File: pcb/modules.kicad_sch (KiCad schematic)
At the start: 12 parts, among them IC2 E22-900M22S, J2 Conn_01x08_Pin, J3 Conn_Coaxial, J4 Conn_Coaxial, U4 BME280, U6 NEO-M8M

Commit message: Updating schematic & pcb & BOM
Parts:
- J3: footprint (none) -> Connector_Coaxial:U.FL_Hirose_U.FL-R-SMT-1_Vertical
- L2: footprint (none) -> Inductor_SMD:L_0805_2012Metric
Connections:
- net +3V3: now also J2.7 (Pin_7)
- net GND: now also J2.8 (Pin_8)
- net SCL: now also J2.6 (Pin_6)
- net SDA: now also J2.5 (Pin_5)
- net BLK: now reaches J2.1 (Pin_1)
- net CS: now reaches J2.2 (Pin_2)
- net DC: now reaches J2.3 (Pin_3)
- net RES: now reaches J2.4 (Pin_4)
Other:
- title: (none) -> NOMAD MODULES
- moved on the sheet: C9, D2, IC2, J2, J3, J4, L2, R14, R16, R17, U4, U6

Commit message: Updating PCB
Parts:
- added Q1: NPN, symbol Simulation_SPICE:NPN
- added R1: R, symbol Device:R
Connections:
- net +3V3: now also IC2.9 (VCC), R1.2
- net GND: now also D2.1 (K), J4.2 (Ext)
- net at D2.2 (A): now also Q1.3 (E)
- new net: Q1.1 (C), R1.1
- new net FLASHLIGHT: Q1.2 (B)
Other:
- moved on the sheet: D2

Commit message: Updating footprints, PCb and schematics.
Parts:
- R1: footprint (none) -> Resistor_SMD:R_0805_2012Metric
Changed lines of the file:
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@@
 			)
 		)
-		(property "Footprint" ""
+		(property "Footprint" "Resistor_SMD:R_0805_2012Metric"
 			(at 201.422 144.78 90)
 			(hide yes)

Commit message: Updating PCB
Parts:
- removed Q1: NPN, symbol Simulation_SPICE:NPN
- added Q2: 2N7002, Package_TO_SOT_SMD:SOT-23, symbol Transistor_FET:2N7002
- added R19: 100R, symbol Device:R
- R1: value R -> 1.5k
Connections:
- net +3V3: now also D2.1 (K); no longer R1.2
- net FLASHLIGHT: now also R19.2
- net GND: now also R1.1; no longer D2.1 (K)
- net at D2.2 (A): now also Q2.3 (D)
- new net: Q2.2 (S), R1.2
- new net: Q2.1 (G), R19.1
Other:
- moved on the sheet: D2, R1

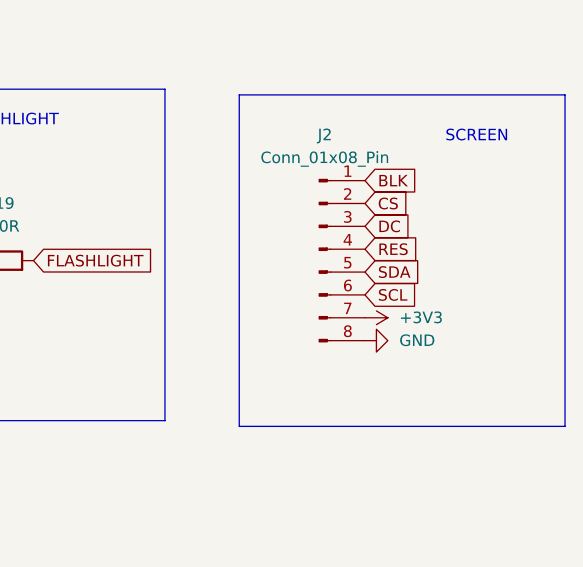
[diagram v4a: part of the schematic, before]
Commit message: Updating PCB: Adding Buck boost converter, battery protection and other fixes.
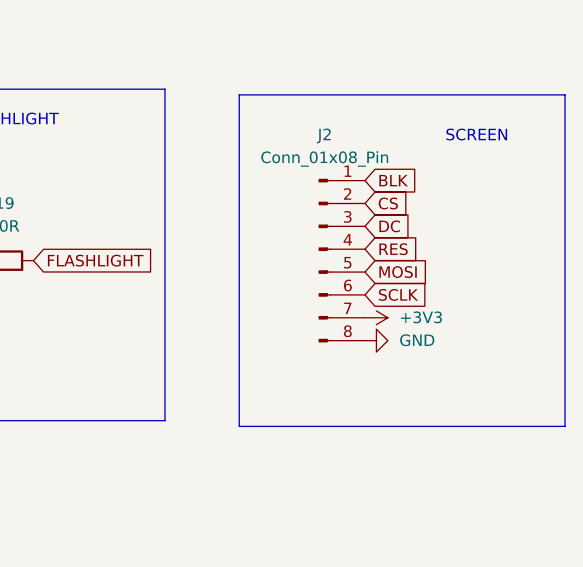
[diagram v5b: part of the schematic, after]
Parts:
- R19: footprint (none) -> Resistor_SMD:R_0805_2012Metric
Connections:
- net SCL: no longer J2.6 (Pin_6)
- net SDA: no longer J2.5 (Pin_5)
- new net MOSI: J2.5 (Pin_5)
- new net SCLK: J2.6 (Pin_6)

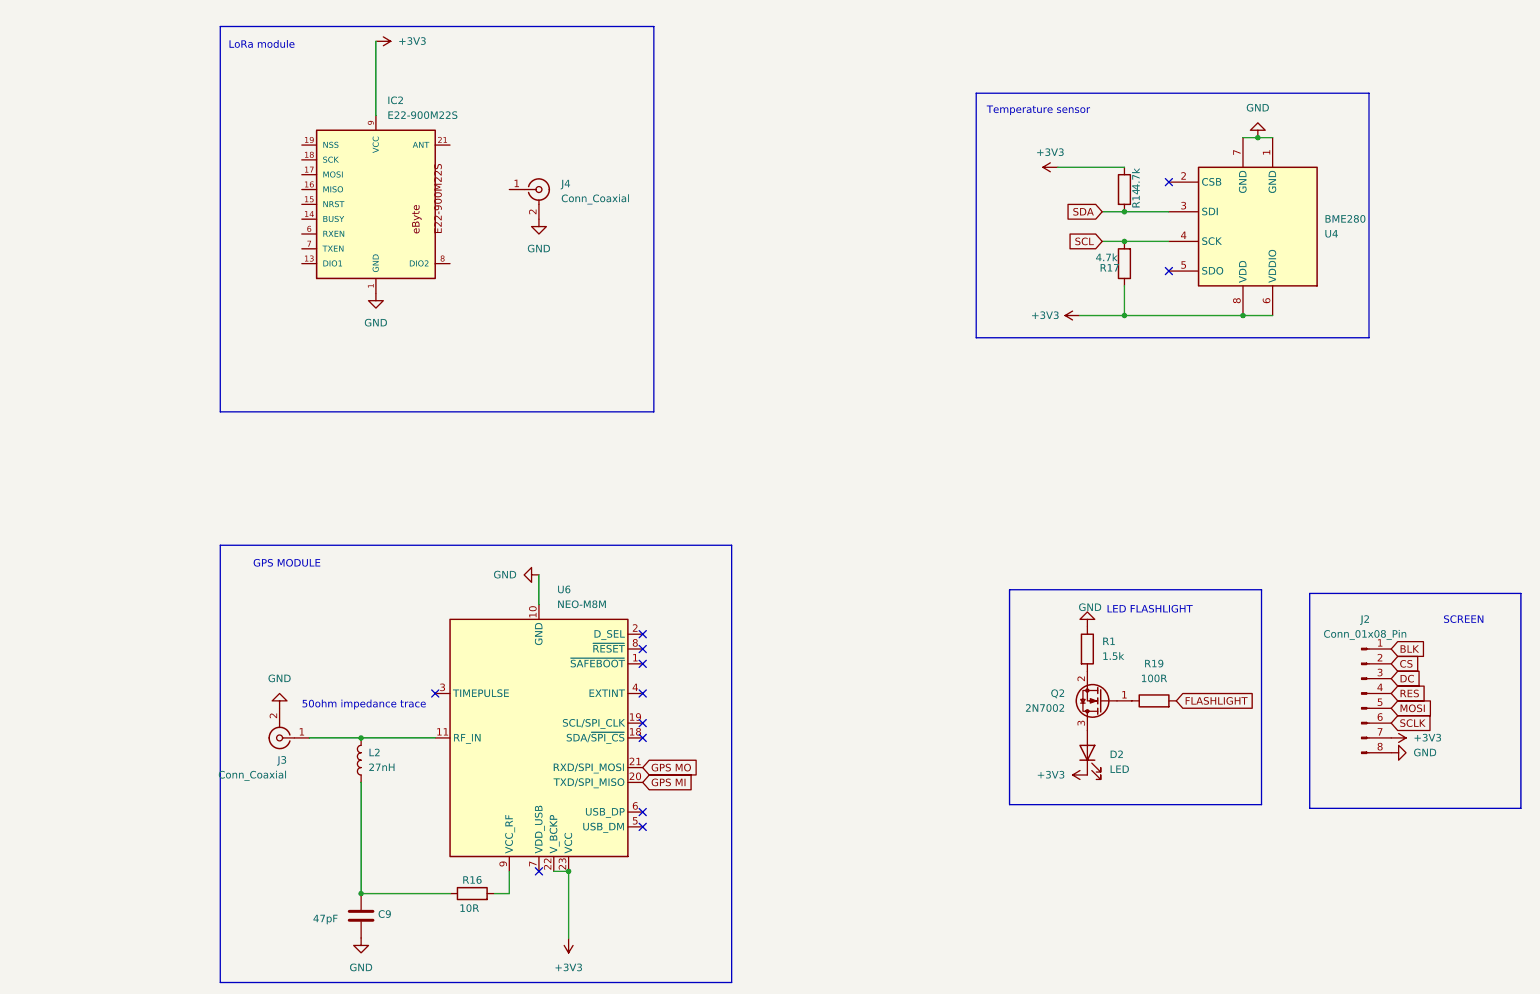
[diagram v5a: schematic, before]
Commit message: Adding NEO-M8N module schematic + BME280 schematic
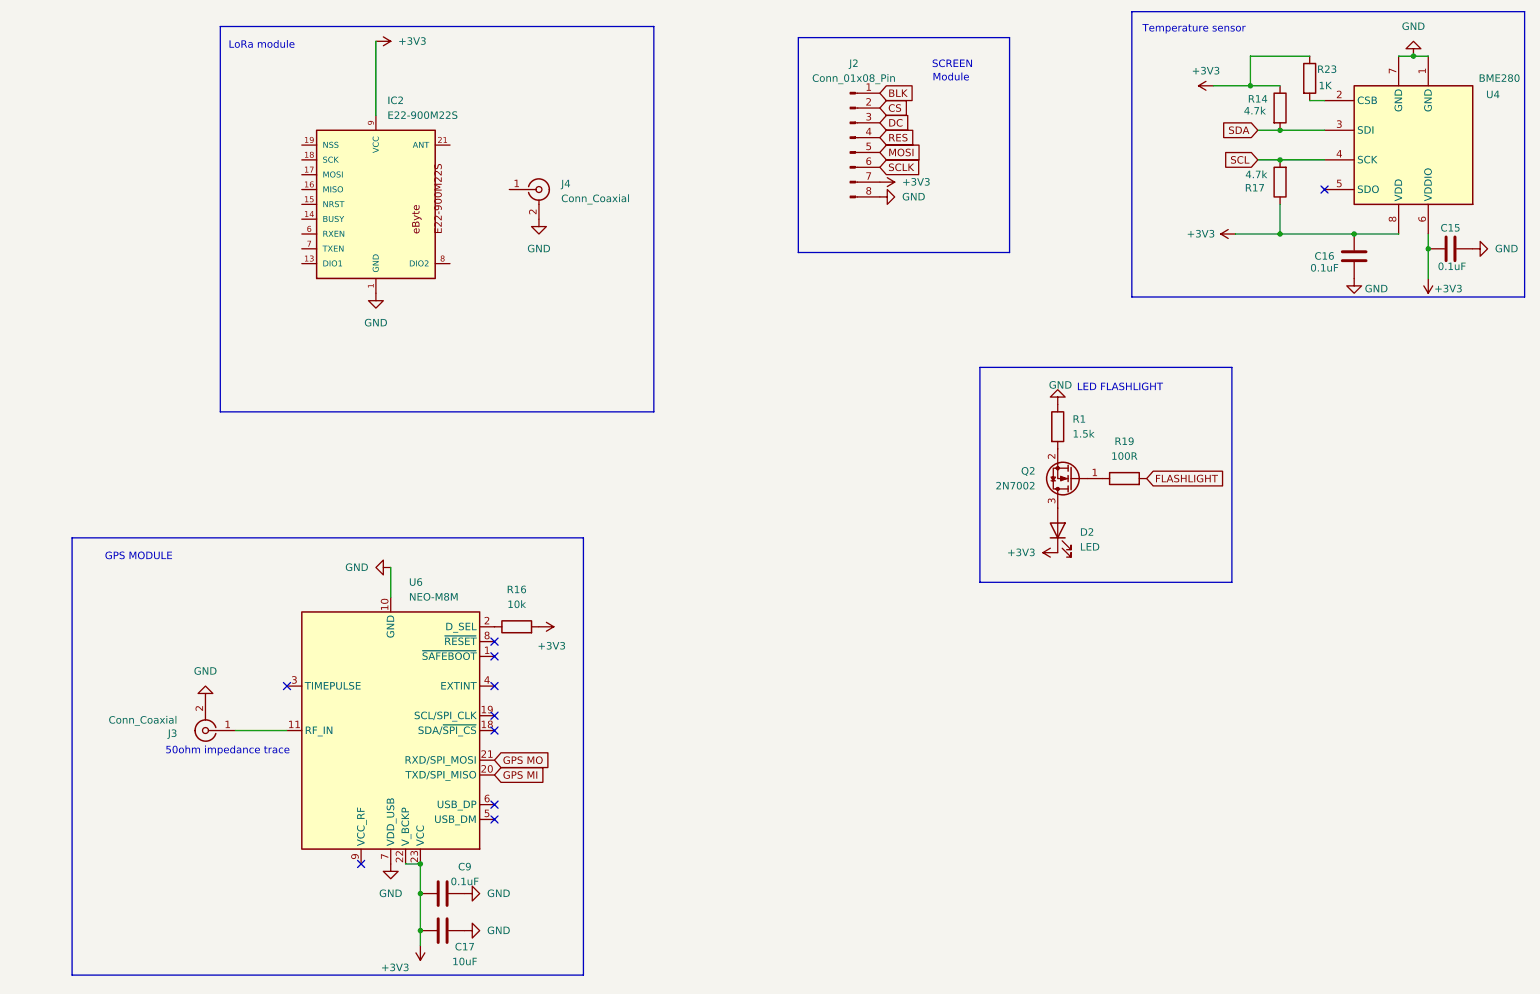
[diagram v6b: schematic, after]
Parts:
- removed L2: 27nH, Inductor_SMD:L_0805_2012Metric, symbol Device:L
- added C15, C16: 0.1uF, symbol Device:C
- added C17: 10uF, symbol Device:C
- added R23: 1K, symbol Device:R
- C9: value 47pF -> 0.1uF; footprint Capacitor_SMD:C_0805_2012Metric -> (none)
- J3: footprint Connector_Coaxial:U.FL_Hirose_U.FL-R-SMT-1_Vertical -> Connector_Coaxial:SMA_Molex_73251-1153_EdgeMount_Horizontal
- R16: value 10R -> 10k; footprint Resistor_SMD:R_0805_2012Metric -> (none)
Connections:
- net +3V3: now also C9.1, R16.2, C15.1, C16.1, C17.1, R23.1
- net GND: now also C9.2, U6.7 (VDD_USB), C15.2, C16.2, C17.2; no longer C9.1
- net at R16.1: now also U6.2 (D_SEL); no longer C9.2
- net at U6.9 (VCC_RF): no longer R16.2
- net at U4.2 (CSB): now also R23.2
- no-connect marks 12 -> 10
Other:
- note added: "Module"
- moved on the sheet: D2, J2, J3, Q2, R1, R14, R17, R19, U4, U6

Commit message: Adding LoRa module schematic
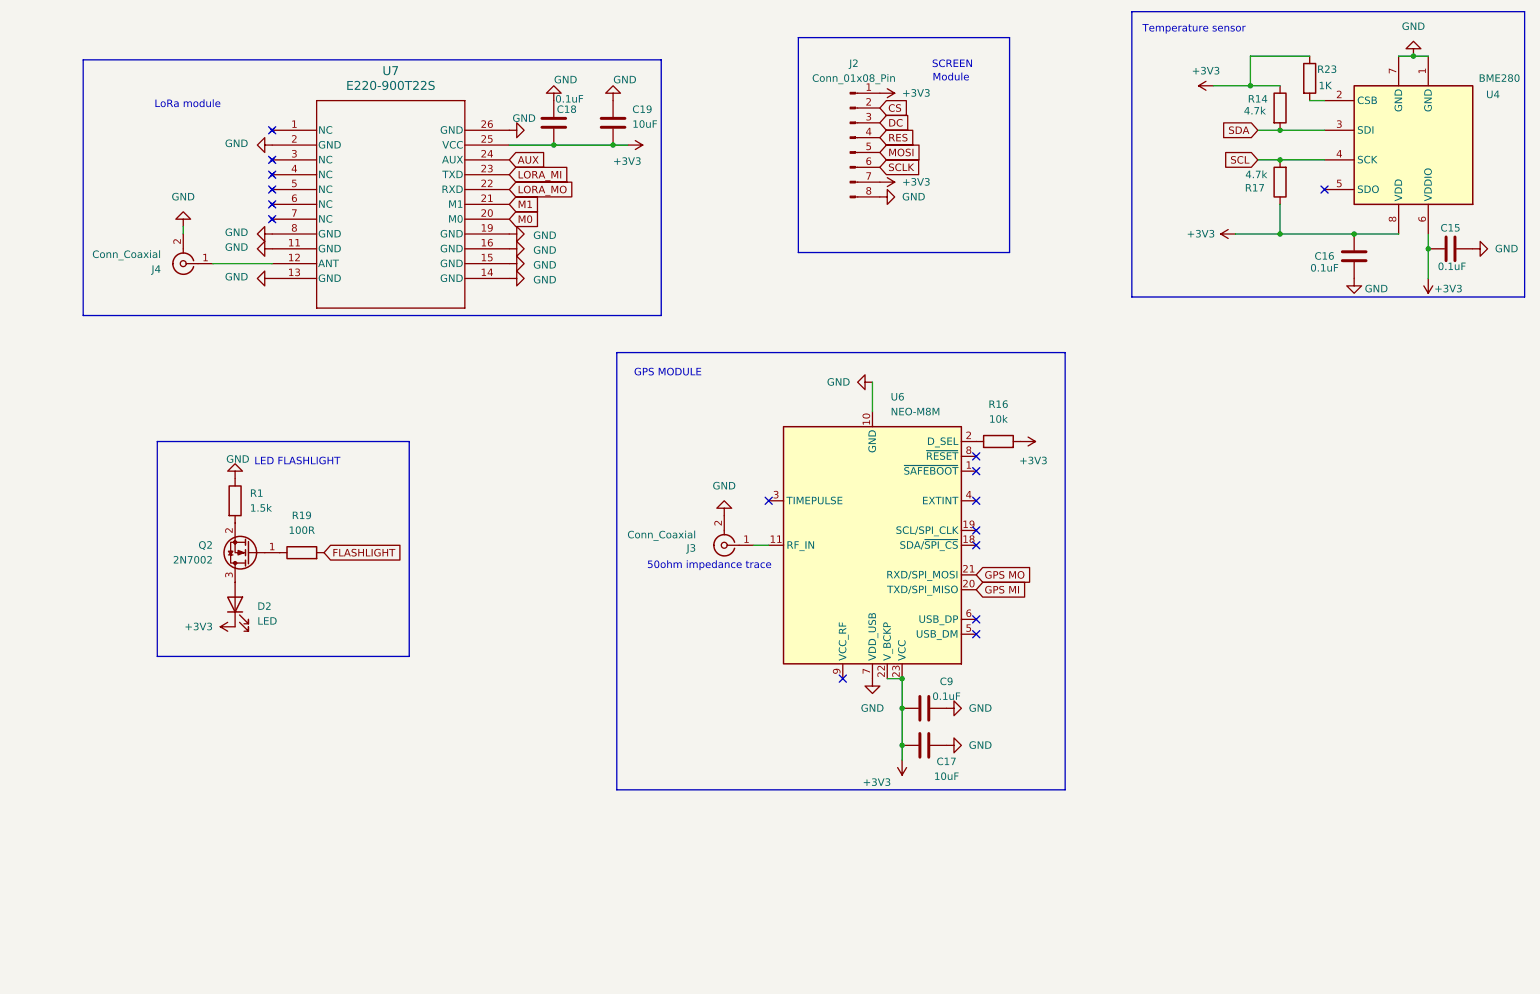
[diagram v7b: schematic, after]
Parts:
- removed IC2: E22-900M22S, E22-900M22S:E22-900M22S, symbol E22-900M22S:E22-900M22S
- added C18: 0.1uF, Capacitor_SMD:C_0805_2012Metric, symbol Device:C
- added C19: 10uF, Capacitor_SMD:C_0805_2012Metric, symbol Device:C
- added U7: E220-900T22S, E220-900T22S_BYT, symbol 2026-06-15_15-42-26:E220-900T22S
- C15, C16, C17, C9: footprint (none) -> Capacitor_SMD:C_0805_2012Metric
- R16, R23: footprint (none) -> Resistor_SMD:R_0805_2012Metric
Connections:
- net BLK is gone; now on net +3V3: J2.1 (Pin_1)
- net +3V3: now also C18.2, C19.2, U7.25 (VCC)
- net GND: now also C18.1, C19.1, U7.11 (GND), U7.13 (GND), U7.14 (GND), U7.15 (GND), U7.16 (GND), U7.19 (GND), U7.2 (GND), U7.26 (GND), U7.8 (GND)
- net at J4.1 (In): now also U7.12 (ANT)
- new net AUX: U7.24 (AUX)
- new net LORA_MI: U7.23 (TXD)
- new net LORA_MO: U7.22 (RXD)
- new net M0: U7.20 (M0)
- new net M1: U7.21 (M1)
- no-connect marks 10 -> 16
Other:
- moved on the sheet: C17, C9, D2, J3, J4, Q2, R1, R16, R19, U6
